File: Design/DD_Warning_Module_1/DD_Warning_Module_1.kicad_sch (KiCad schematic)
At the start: 29 parts, among them J1 Conn_01x04, J2 BL_3

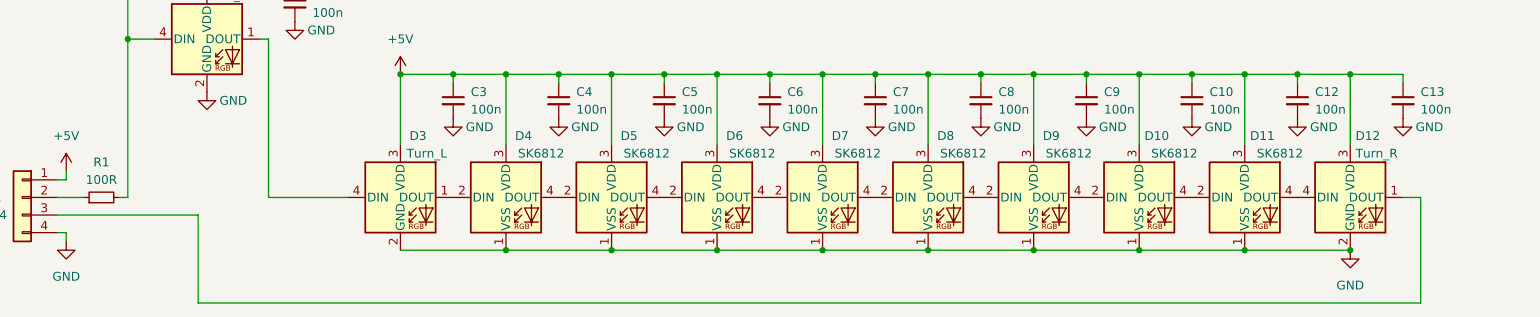
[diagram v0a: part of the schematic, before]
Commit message: warning module update; ws2812->ws2813 (backup data in)
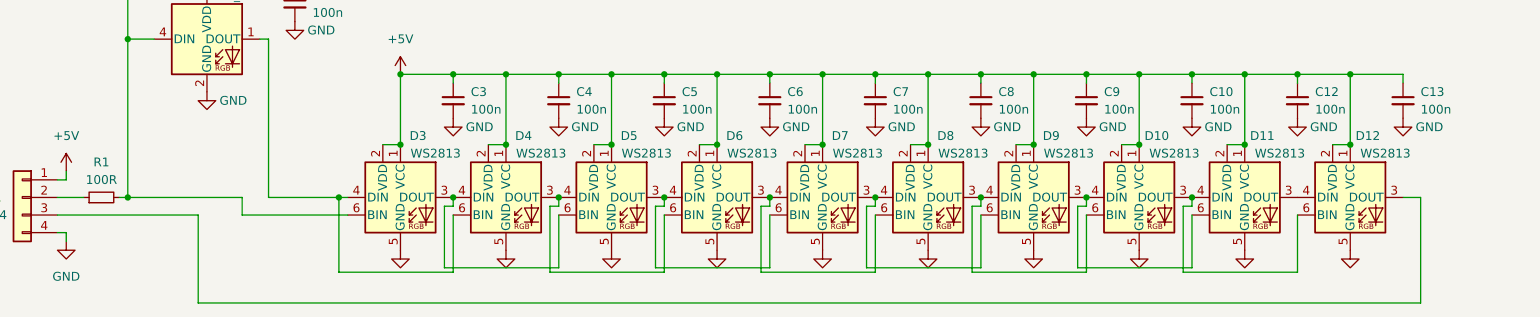
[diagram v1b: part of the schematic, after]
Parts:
- removed D12: Turn_R, LED_THT:LED_D5.0mm-4_RGB, symbol LED:NeoPixel_THT
- removed D3: Turn_L, LED_THT:LED_D5.0mm-4_RGB, symbol LED:NeoPixel_THT
- added D12, D3: WS2813, LED_SMD:LED_WS2812_PLCC6_5.0x5.0mm_P1.6mm, symbol LED:WS2813
- D10, D11, D4, D5, D6, D7, D8, D9: value SK6812 -> WS2813; footprint LED_SMD:LED_SK6812_PLCC4_5.0x5.0mm_P3.2mm -> LED_SMD:LED_WS2812_PLCC6_5.0x5.0mm_P1.6mm; symbol LED:SK6812 -> LED:WS2813
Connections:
- net +5V: now also D10.1 (VCC), D10.2 (VDD), D11.1 (VCC), D11.2 (VDD), D4.1 (VCC), D4.2 (VDD), D5.1 (VCC), D5.2 (VDD), D6.1 (VCC), D6.2 (VDD), D7.1 (VCC), D7.2 (VDD), D8.1 (VCC), D8.2 (VDD), D9.1 (VCC), D9.2 (VDD), D12.1 (VCC), D12.2 (VDD), D3.1 (VCC), D3.2 (VDD); no longer D10.3 (VDD), D11.3 (VDD), D4.3 (VDD), D5.3 (VDD), D6.3 (VDD), D7.3 (VDD), D8.3 (VDD), D9.3 (VDD)
- net GND: now also D10.5 (GND), D11.5 (GND), D4.5 (GND), D5.5 (GND), D6.5 (GND), D7.5 (GND), D8.5 (GND), D9.5 (GND), D12.5 (GND), D3.5 (GND); no longer D10.1 (VSS), D11.1 (VSS), D4.1 (VSS), D5.1 (VSS), D6.1 (VSS), D7.1 (VSS), D8.1 (VSS), D9.1 (VSS)
- net at D8.4 (DIN): now also D7.3 (DOUT), D9.6 (BIN); no longer D9.2 (DIN)
- net at D9.4 (DIN): now also D10.6 (BIN), D8.3 (DOUT); no longer D10.2 (DIN)
- net at D10.4 (DIN): now also D11.6 (BIN), D9.3 (DOUT); no longer D11.2 (DIN)
- net at D2.1 (DOUT): now also D4.6 (BIN), D3.4 (DIN)
- net at D1.4 (DIN), D2.4 (DIN), J2.2 (Pin_2)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: now also D3.6 (BIN)
- net at D6.4 (DIN): now also D5.3 (DOUT), D7.6 (BIN); no longer D7.2 (DIN)
- net at D7.4 (DIN): now also D6.3 (DOUT), D8.6 (BIN); no longer D8.2 (DIN)
- net at D11.4 (DIN): now also D10.3 (DOUT), D12.6 (BIN)
- net at D4.4 (DIN): now also D5.6 (BIN), D3.3 (DOUT); no longer D5.2 (DIN)
- net at D5.4 (DIN): now also D4.3 (DOUT), D6.6 (BIN); no longer D6.2 (DIN)
- net at J1.3 (Pin_3): now also D12.3 (DOUT)
- new net: D11.3 (DOUT), D12.4 (DIN)
